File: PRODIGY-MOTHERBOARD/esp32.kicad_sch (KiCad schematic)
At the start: 7 parts, among them J25 Bus_M.2_Socket_B, P1 USB_C_Plug, SW2 SW_Push_Dual_x2

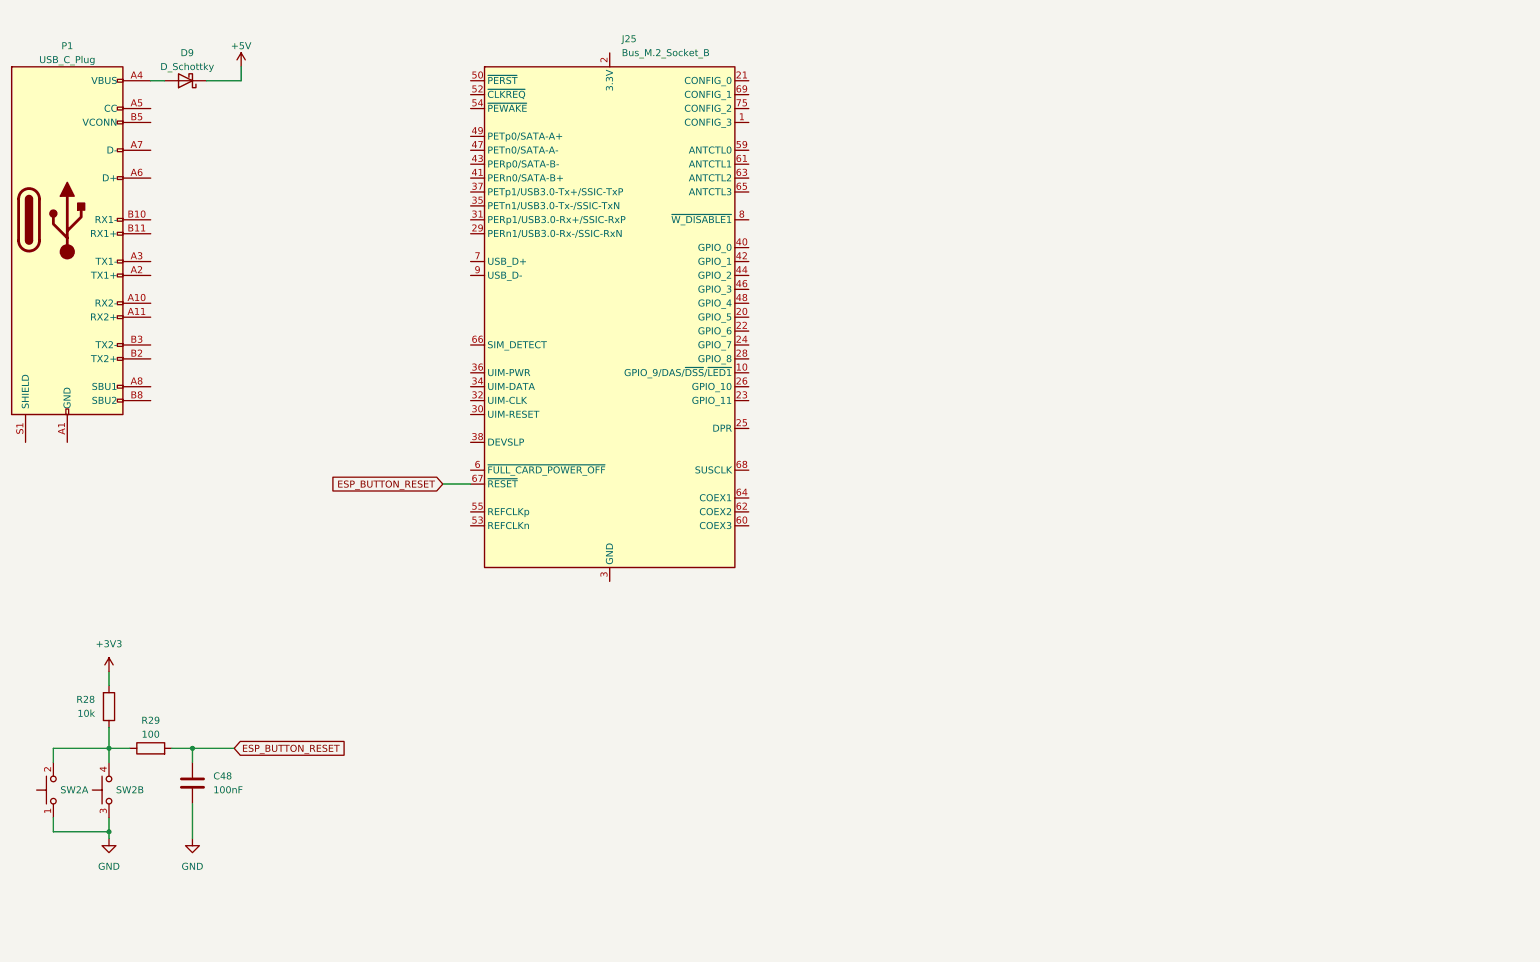
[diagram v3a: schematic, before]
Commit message: Added pins to MCU. Added Decoder for SPI SS-Multiplexing.
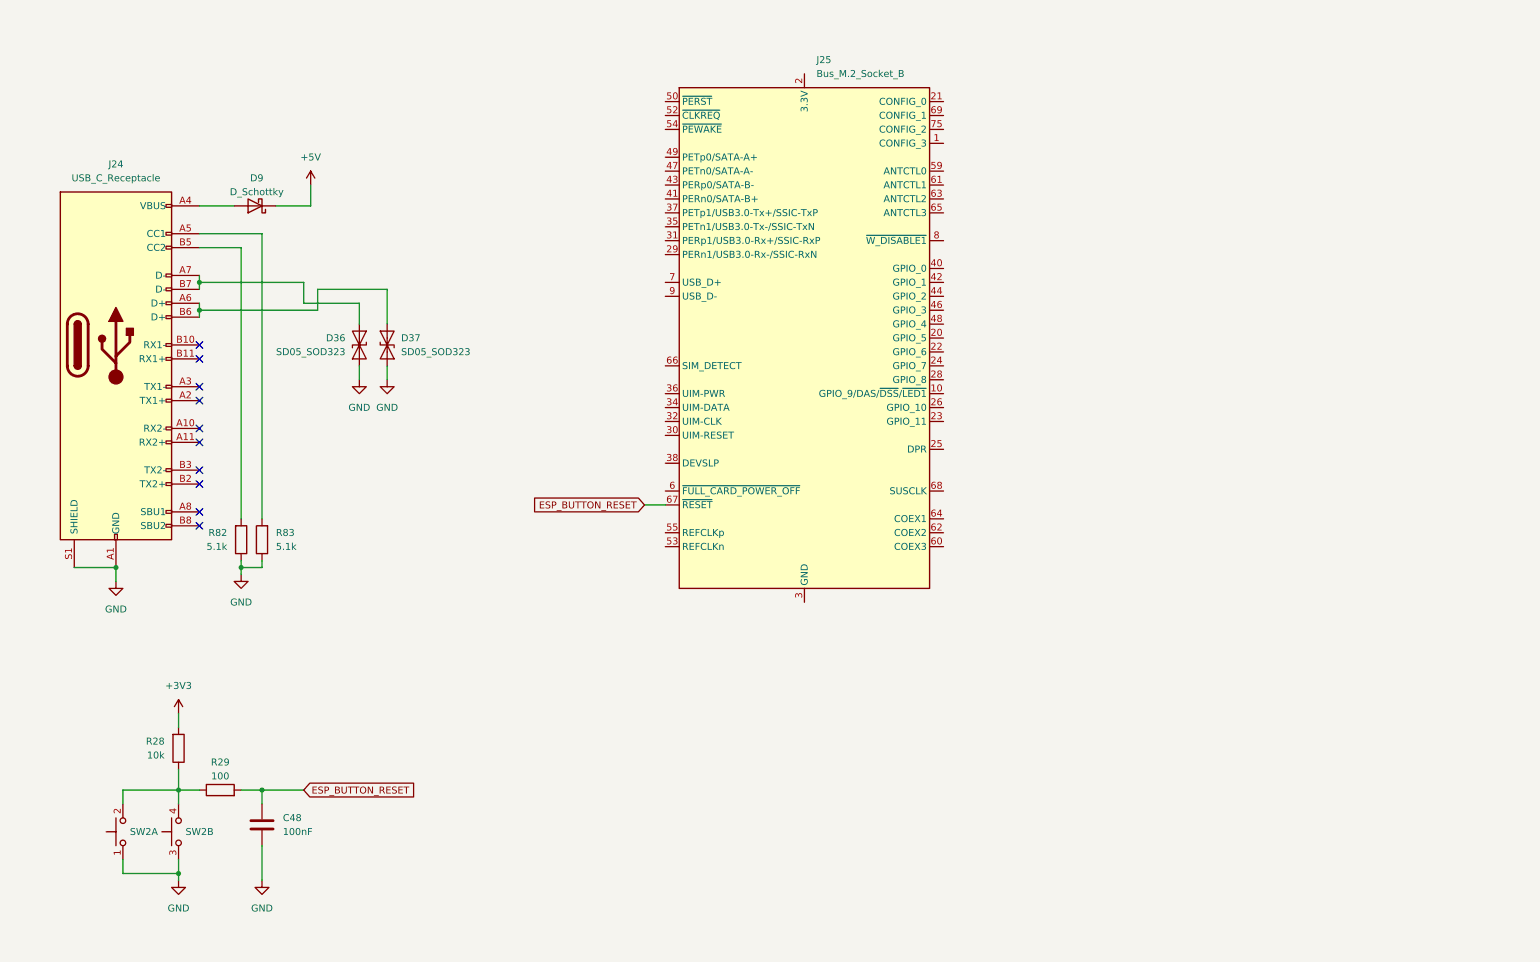
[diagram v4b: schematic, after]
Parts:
- removed P1: USB_C_Plug, Connector_USB:USB_C_Receptacle_GCT_USB4105-xx-A_16P_TopMnt_Horizontal, symbol Connector:USB_C_Plug
- added D36, D37: SD05_SOD323, Diode_SMD:D_SOD-323, symbol Diode:SD05_SOD323
- added J24: USB_C_Receptacle, symbol Connector:USB_C_Receptacle
- added R82, R83: 5.1k, Resistor_SMD:R_0603_1608Metric, symbol Device:R
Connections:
- net GND: now also D36.1 (A1), D37.1 (A1), J24.A1 (GND), J24.A12 (GND), J24.B1 (GND), J24.B12 (GND), J24.S1 (SHIELD), R82.1, R83.1
- net at D9.2 (A): now also J24.A4 (VBUS), J24.A9 (VBUS), J24.B4 (VBUS), J24.B9 (VBUS)
- new net: J24.B5 (CC2), R82.2
- new net: J24.A5 (CC1), R83.2
- new net: D37.2 (A2), J24.A6 (D+), J24.B6 (D+)
- new net: D36.2 (A2), J24.A7 (D-), J24.B7 (D-)
- no-connect marks 0 -> 10
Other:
- moved on the sheet: C48, J25, R28, R29, SW2A, SW2B

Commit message: Added proper debounce filter elements to buttons.
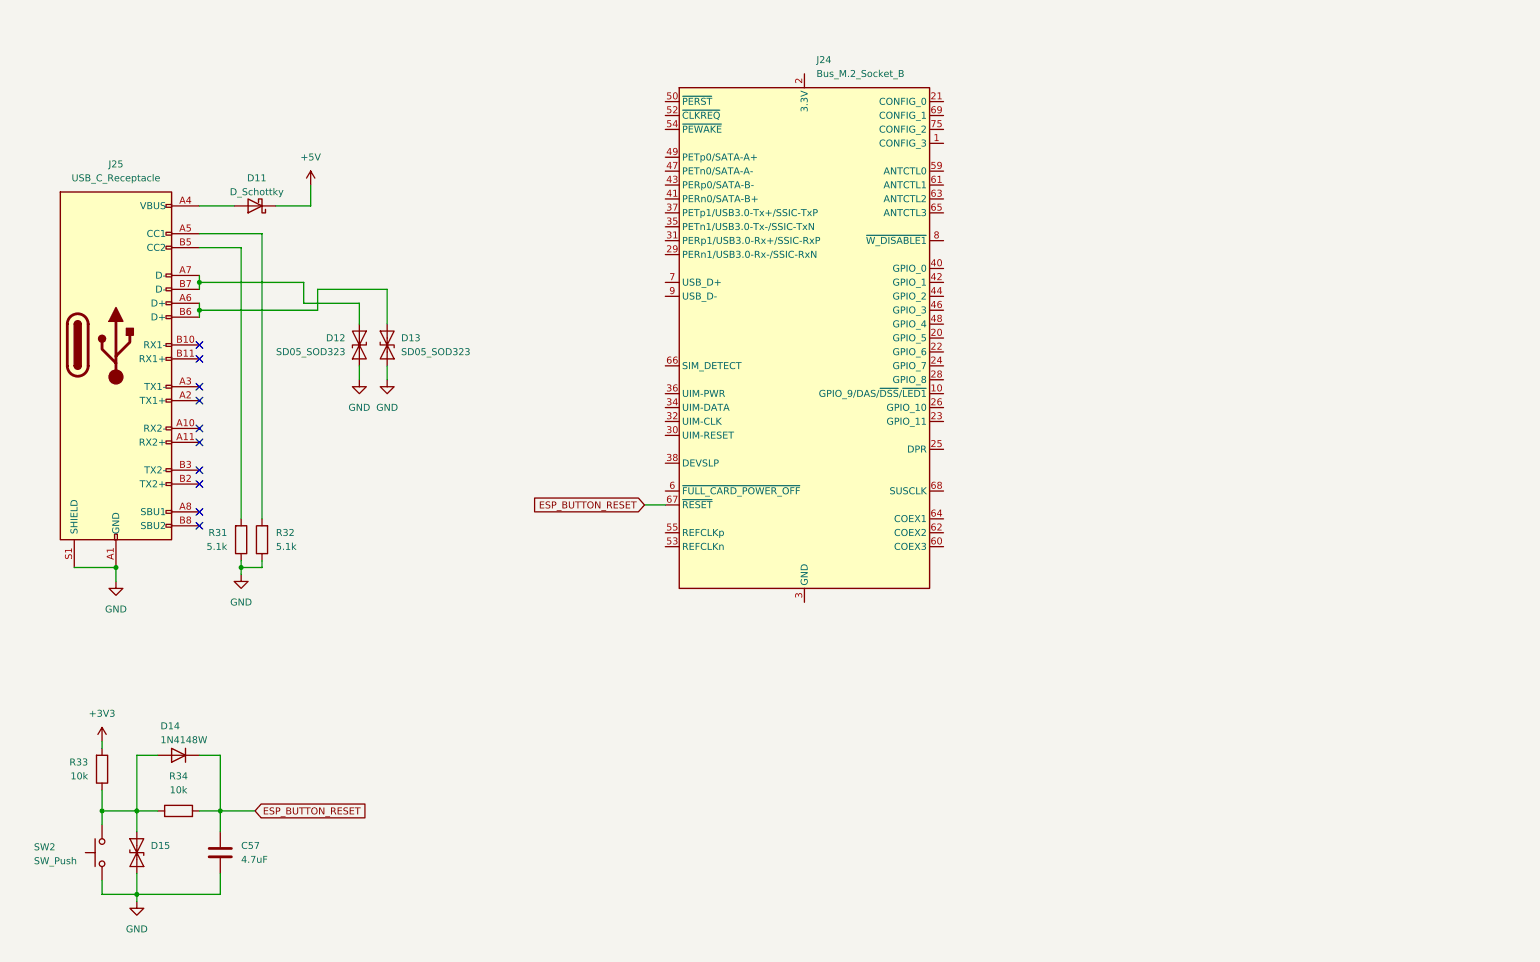
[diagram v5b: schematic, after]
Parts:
- removed C48: 100nF, symbol Device:C
- removed R28: 10k, Resistor_SMD:R_0603_1608Metric, symbol Device:R
- removed R29: 100, Resistor_SMD:R_0603_1608Metric, symbol Device:R
- removed SW2: SW_Push_Dual_x2, symbol Switch:SW_Push_Dual_x2
- added C57: 4.7uF, symbol Device:C
- added D14: 1N4148W, Diode_SMD:D_SOD-123, symbol Diode:1N4148W
- added D15: SD05_SOD323, Diode_SMD:D_SOD-323, symbol Diode:SD05_SOD323
- added R33, R34: 10k, Resistor_SMD:R_0603_1608Metric, symbol Device:R
- added SW2: SW_Push, Button_Switch_SMD:SW_Push_1P1T_NO_CK_KMR2, symbol Switch:SW_Push
- renumbered D9 to D11, D36 to D12, D37 to D13, J25 to J24, J24 to J25, R82 to R31, R83 to R32
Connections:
- net +3V3: now also R33.2
- net ESP_BUTTON_RESET: now also C57.1, D14.1 (K), R34.2
- net GND: now also C57.2, D15.1 (A1), SW2.1
- new net: D14.2 (A), D15.2 (A2), R33.1, R34.1, SW2.2

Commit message: Esp32 motherboard schematic done.
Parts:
- added J28: Conn_02x20_Odd_Even, Connector_PinHeader_2.54mm:PinHeader_2x20_P2.54mm_Horizontal, symbol Connector_Generic:Conn_02x20_Odd_Even
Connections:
- net +3V3: now also J24.2 (3.3V), J24.4 (3.3V), J24.70 (3.3V), J24.72 (3.3V), J24.74 (3.3V), J28.1 (Pin_1), J28.17 (Pin_17)
- net +5V: now also J28.2 (Pin_2), J28.4 (Pin_4)
- net ESP_BUTTON_RESET: now also J28.40 (Pin_40)
- net GND: now also J24.11 (GND), J24.27 (GND), J24.3 (GND), J24.33 (GND), J24.39 (GND), J24.45 (GND), J24.5 (GND), J24.51 (GND), J24.57 (GND), J24.71 (GND), J24.73 (GND), J28.14 (Pin_14), J28.20 (Pin_20), J28.25 (Pin_25), J28.30 (Pin_30), J28.34 (Pin_34), J28.39 (Pin_39), J28.6 (Pin_6), J28.9 (Pin_9)
- net at D13.2 (A2), J25.A6 (D+), J25.B6 (D+): now also J24.7 (USB_D+)
- net at D12.2 (A2), J25.A7 (D-), J25.B7 (D-): now also J24.9 (USB_D-)
- net ESP_GPIO_35: now reaches J24.1 (CONFIG_3)
- net ESP_GPIO_35: now also J28.36 (Pin_36)
- net ESP_GPIO_11: now reaches J24.10 (GPIO_9/DAS/~{DSS}/~{LED1})
- net ESP_GPIO_11: now also J28.18 (Pin_18)
- net ESP_GPIO_16: now reaches J24.20 (GPIO_5)
- net ESP_GPIO_16: now also J28.8 (Pin_8)
- net ESP_GPIO_38: now reaches J24.21 (CONFIG_0)
- net ESP_GPIO_38: now also J24.60 (COEX3), J28.7 (Pin_7)
- net ESP_GPIO_8: now reaches J24.22 (GPIO_6)
- net ESP_GPIO_8: now also J28.10 (Pin_10)
- net ESP_GPIO_13: now reaches J24.23 (GPIO_11)
- net ESP_GPIO_13: now also J28.24 (Pin_24)
- net ESP_GPIO_9: now reaches J24.24 (GPIO_7)
- net ESP_GPIO_9: now also J28.12 (Pin_12)
- net ESP_GPIO_12: now reaches J24.26 (GPIO_10)
- net ESP_GPIO_12: now also J28.22 (Pin_22)
- net ESP_GPIO_10: now reaches J24.28 (GPIO_8)
- net ESP_GPIO_10: now also J28.16 (Pin_16)
- net ESP_SERIAL_RX0: now reaches J24.30 (UIM-RESET)
- net ESP_SERIAL_RX0: now also J28.37 (Pin_37)
- net ESP_SERIAL_TX0: now reaches J24.32 (UIM-CLK)
- net ESP_SERIAL_TX0: now also J28.35 (Pin_35)
- net SERIAL_ESP_RX1: now reaches J24.34 (UIM-DATA)
- net SERIAL_ESP_TX1: now reaches J24.36 (UIM-PWR)
- net ESP_GPIO_4: now reaches J24.40 (GPIO_0)
- net ESP_GPIO_4: now also J28.21 (Pin_21)
- net ESP_GPIO_5: now reaches J24.42 (GPIO_1)
- net ESP_GPIO_5: now also J28.23 (Pin_23)
- net ESP_GPIO_6: now reaches J24.44 (GPIO_2)
- net ESP_GPIO_6: now also J28.29 (Pin_29)
- net ESP_GPIO_7: now reaches J24.46 (GPIO_3)
- net ESP_GPIO_7: now also J28.31 (Pin_31)
- net ESP_GPIO_15: now reaches J24.48 (GPIO_4)
- net ESP_GPIO_15: now also J28.33 (Pin_33)
- net ESP_GPIO_14: now reaches J24.59 (ANTCTL0)
- net ESP_GPIO_14: now also J28.11 (Pin_11)
- net ESP_GPIO_21: now reaches J24.61 (ANTCTL1)
- net ESP_GPIO_21: now also J28.13 (Pin_13)
- net ESP_GPIO_2: now reaches J24.62 (COEX2)
- net ESP_GPIO_2: now also J28.5 (Pin_5)
- net ESP_GPIO_47: now reaches J24.63 (ANTCTL2)
- net ESP_GPIO_47: now also J28.15 (Pin_15)
- net ESP_GPIO_1: now reaches J24.64 (COEX1)
- net ESP_GPIO_1: now also J28.3 (Pin_3)
- net ESP_GPIO_48: now reaches J24.65 (ANTCTL3)
- net ESP_GPIO_48: now also J28.19 (Pin_19)
- net ESP_BUTTON_BOOT: now reaches J24.68 (SUSCLK)
- net ESP_BUTTON_BOOT: now also J28.38 (Pin_38)
- net ESP_GPIO_37: now reaches J24.69 (CONFIG_1)
- net ESP_GPIO_37: now also J28.26 (Pin_26)
- net ESP_GPIO_36: now reaches J24.75 (CONFIG_2)
- net ESP_GPIO_36: now also J28.32 (Pin_32)
- no-connect marks 10 -> 26
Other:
- note added: "PSRAM"
- note added: "RESET Button"
- note added: "Raspberry Pi compatible GPIO breakout"
- note added: "USB CDC Mode"
- note added: "USB-C USB 2.0"
- moved on the sheet: J24

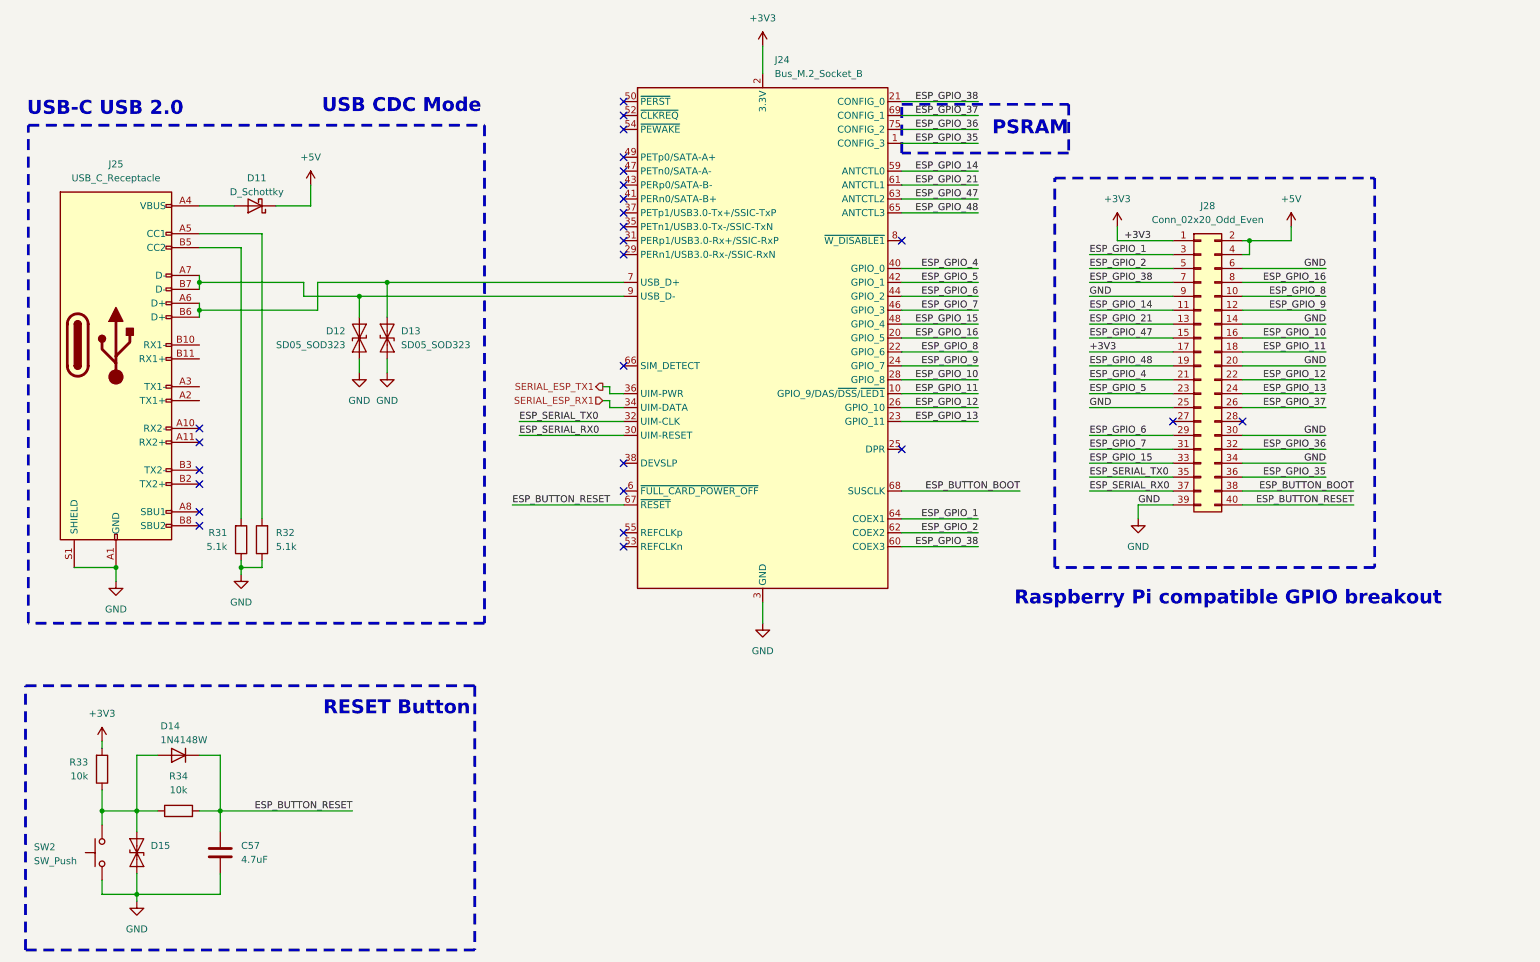
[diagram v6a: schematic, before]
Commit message: Submitted V0 for evaluation. Avaiting feedback.
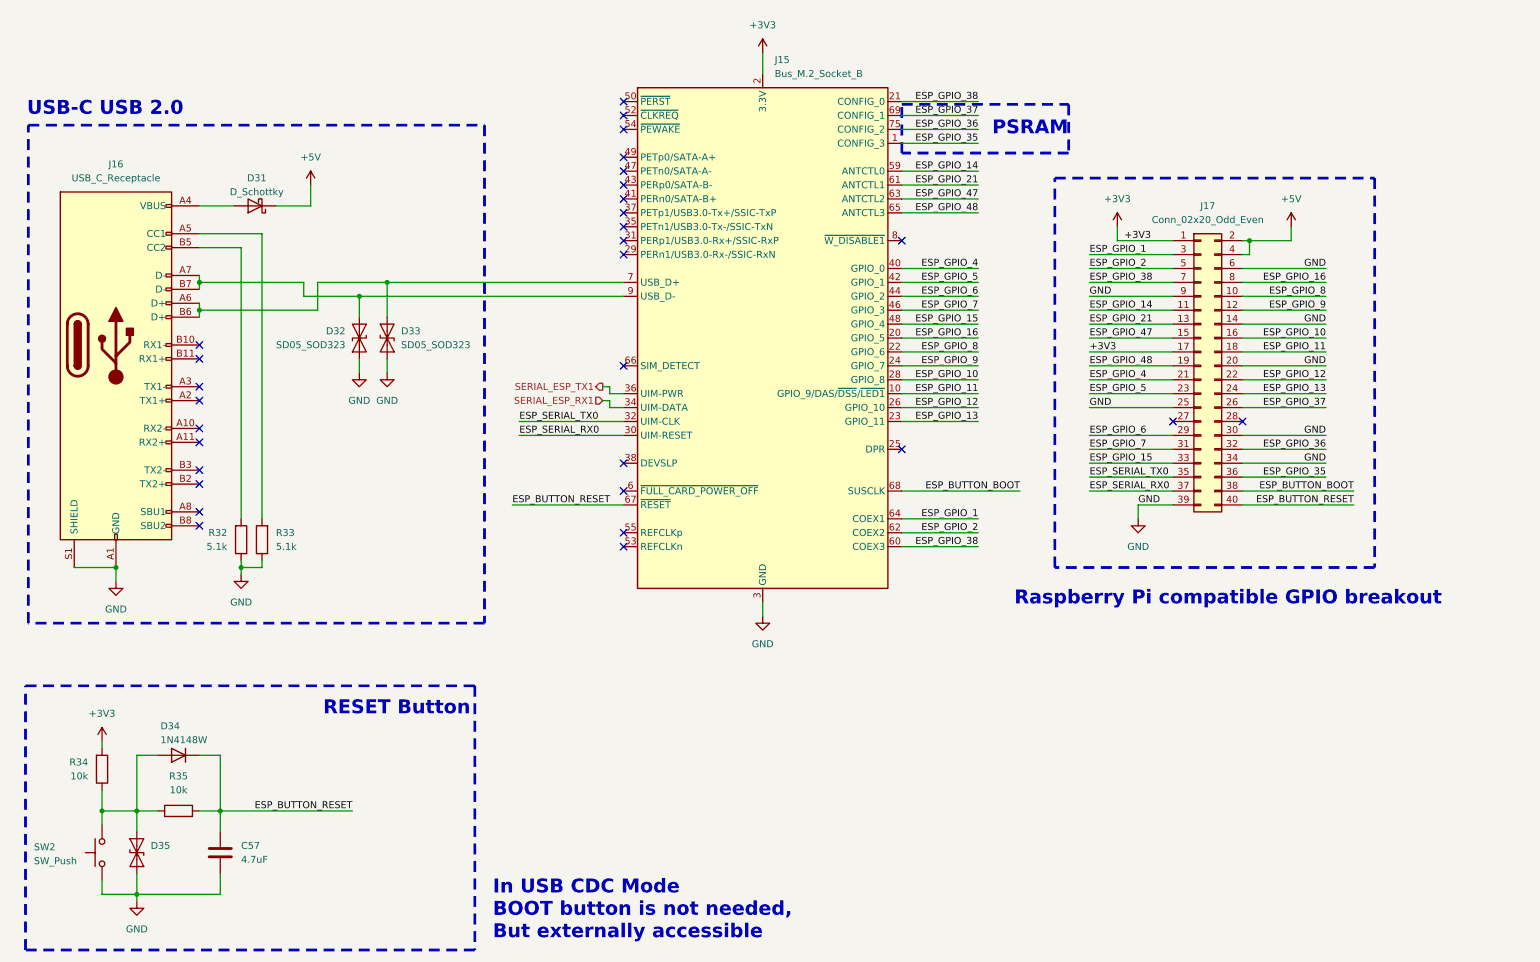
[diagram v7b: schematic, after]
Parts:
- renumbered D11 to D31, D12 to D32, D13 to D33, D14 to D34, D15 to D35, J24 to J15, J25 to J16, J28 to J17, R31 to R32, R32 to R33, R33 to R34, R34 to R35
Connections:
- no-connect marks 26 -> 30
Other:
- note added: "In USB CDC Mode BOOT button is not needed, But externally accessible"
- note removed: "USB CDC Mode"

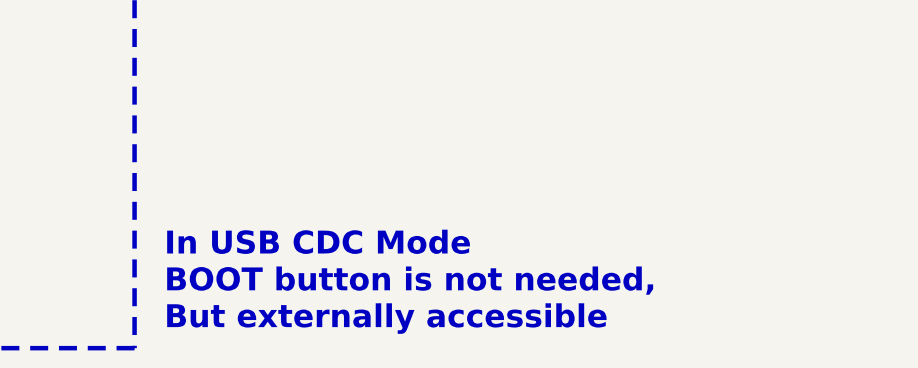
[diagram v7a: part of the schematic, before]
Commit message: MCU schematic done. Started Analog design.
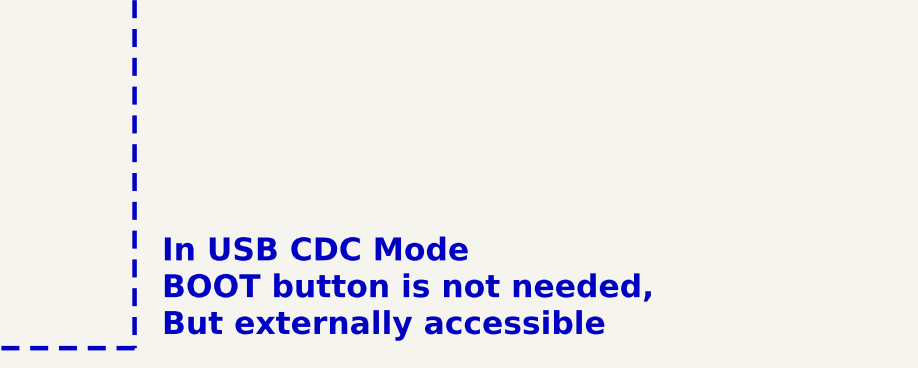
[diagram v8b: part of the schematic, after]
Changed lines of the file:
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@@
 	(text "In USB CDC Mode\nBOOT button is not needed,\nBut externally accessible"
 		(exclude_from_sim no)
-		(at 109.474 189.992 0)
+		(at 109.22 190.754 0)
 		(effects
 			(font
